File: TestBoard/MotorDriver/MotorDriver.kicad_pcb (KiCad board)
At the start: 4 copper layers, 22.2 x 32.5 mm, 14 parts, among them J1 Power Input, J2 Left Rail, J3 Motor Output, J4 Right Rail, U1 DRV8316RRGFR

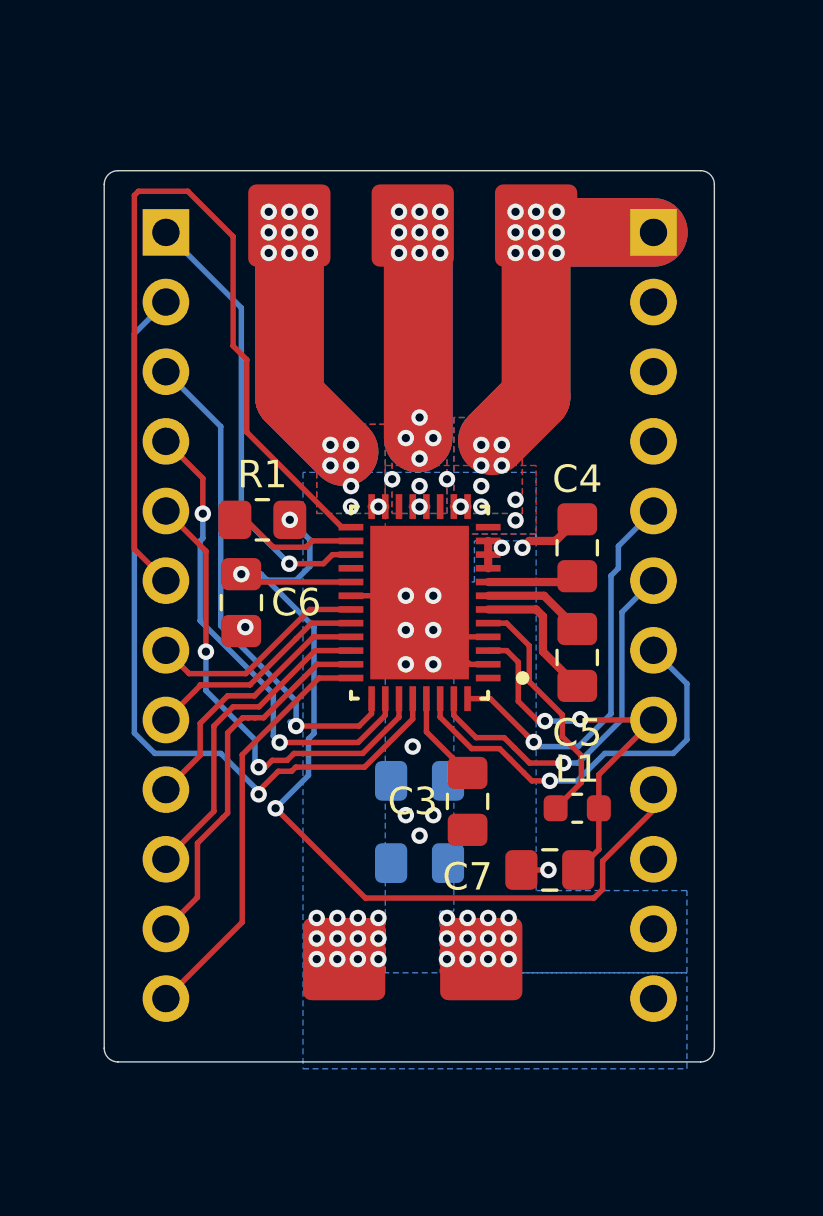
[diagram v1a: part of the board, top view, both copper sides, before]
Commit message: Labeled motor driver
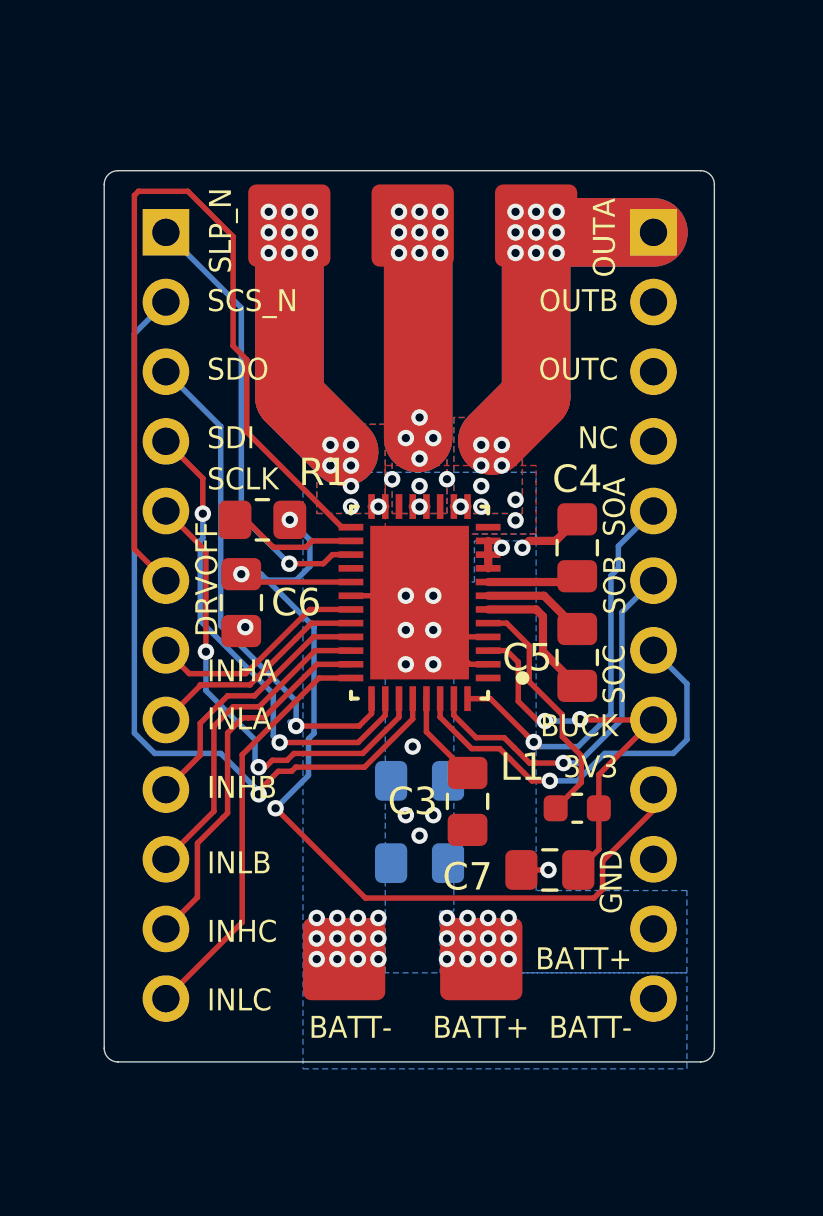
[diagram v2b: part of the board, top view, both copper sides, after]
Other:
- board text added: "3V3"
- board text added: "BATT+"
- board text added: "BATT-"
- board text added: "BUCK"
- board text added: "DRVOFF"
- board text added: "GND"
- board text added: "INHA"
- board text added: "INHB"
- board text added: "INHC"
- board text added: "INLA"
- board text added: "INLB"
- board text added: "INLC"
- board text added: "NC"
- board text added: "OUTA"
- board text added: "OUTB"
- board text added: "OUTC"
- board text added: "SCLK"
- board text added: "SCS_N"
- board text added: "SDI"
- board text added: "SDO"
- board text added: "SLP_N"
- board text added: "SOA"
- board text added: "SOB"
- board text added: "SOC"
